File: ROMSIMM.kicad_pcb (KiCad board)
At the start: 4 copper layers, 88.9 x 19 mm, 8 parts, among them J1 Conn_01x30, U1 511400, U2 511400

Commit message: asdsda
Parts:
- removed the C3 at (118.6, 92.7)
- removed the C3 at (140.2, 92.7)
- added C3: 10u, stdpads:C_0805, F.Cu at (161.8, 105.9)
- added C5: 2u2, stdpads:C_0603, F.Cu at (120.7, 123.4)
- added C6: 2u2, stdpads:C_0603, F.Cu at (120.7, 104.6)
- added H1: MountingHole, Conn:MH_125, F.Cu at (75.1, 117.5)
- added H2: MountingHole, Conn:MH_125, F.Cu at (166.2, 117.5)
- added U3: D15-8, stdpads:PLCC-32_SMDSocket, F.Cu at (130.8, 113.0)
- added U4: D7-0, stdpads:PLCC-32_SMDSocket, F.Cu at (151.1, 113.0)
- C1, C2, C4: value 100n -> 10u; footprint stdpads:C_1206 -> stdpads:C_0805
- J1: value Conn_01x30 -> ROM; footprint stdpads:SIMM-30_Edge -> stdpads:MacIIROMSIMM_Edge
- U1: value 511400 -> D31-24; footprint stdpads:SOJ-24-26-300mil -> stdpads:PLCC-32_SMDSocket
- U2: value 511400 -> D23-16; footprint stdpads:SOJ-24-26-300mil -> stdpads:PLCC-32_SMDSocket
- moved U1 45.8 mm to (90.2, 113.0), turned to 0 degrees
- moved C2 39.5 mm to (79.5, 121.9)
- moved C4 29.2 mm to (161.8, 121.5)
- moved U2 27.9 mm to (110.5, 113.0), turned to 0 degrees
- moved J1 27.8 mm to (120.7, 127.6)
- moved C1 14.2 mm to (79.5, 105.9), turned to 270 degrees
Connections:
- J1 pad 10: /D2 -> GND
- J1 pad 11: /1A6 -> /~CS~
- J1 pad 12: /1A1 -> /~OE~
- J1 pad 13: /D3 -> /~WE~
- J1 pad 14: /1A7 -> /D0
- J1 pad 15: /1A0 -> /D1
- J1 pad 16: /D4 -> /D2
- J1 pad 17: /1A8 -> /D3
- J1 pad 18: /1A10 -> /D4
- J1 pad 19: /1A9 -> /D5
- J1 pad 2: /~CAS~ -> /A0
- J1 pad 20: /D5 -> /D6
- J1 pad 21: /~WE~ -> /D7
- J1 pad 22: GND -> /D8
- J1 pad 23: /D6 -> /D9
- J1 pad 24: /A11 -> /D10
- J1 pad 25: /D7 -> /D11
- J1 pad 26: /QP -> /D12
- J1 pad 27: /~RAS~ -> /D13
- J1 pad 28: /~CASP~ -> /D14
- J1 pad 29: /DP -> /D15
- J1 pad 3: /D0 -> /A1
- J1 pad 30: +5V -> GND
- J1 pad 4: /1A4 -> /A2
- J1 pad 5: /1A3 -> /A3
- J1 pad 6: /D1 -> /A4
- J1 pad 7: /1A5 -> /A5
- J1 pad 8: /1A2 -> /A6
- J1 pad 9: GND -> /A7
- U1 pad 1: +5V -> /A20
- U1 pad 10: /1A1 -> /A4
- U1 pad 11: /1A2 -> /A3
- U1 pad 12: /1A3 -> /A2
- U1 pad 13: +5V -> /D0
- U1 pad 14: GND -> /D1
- U1 pad 15: /1A4 -> /D2
- U1 pad 16: /1A5 -> GND
- U1 pad 17: /1A6 -> /D3
- U1 pad 18: /1A7 -> /D4
- U1 pad 19: /1A8 -> /D5
- U1 pad 2: /D5 -> /A18
- U1 pad 21: /1A9 -> /D7
- U1 pad 22: GND -> /~CS~
- U1 pad 23: /~CAS~ -> /A12
- U1 pad 24: /D6 -> /~OE~
- U1 pad 25: /D4 -> /A13
- U1 pad 26: GND -> /A11
- U1 pad 3: /D7 -> /A17
- U1 pad 4: /~WE~ -> /A14
- U1 pad 5: /~RAS~ -> /A9
- U1 pad 6: Net-(U1-Pad6) -> /A8
- U1 pad 8: /1A10 -> /A6
- U1 pad 9: /1A0 -> /A5
- U2 pad 1: +5V -> /A20
- U2 pad 10: /1A1 -> /A4
- U2 pad 11: /1A0 -> /A3
- U2 pad 12: /1A10 -> /A2
- U2 pad 13: +5V -> /D8
- U2 pad 14: GND -> /D9
- U2 pad 15: /1A9 -> /D10
- U2 pad 16: /1A8 -> GND
- U2 pad 17: /1A7 -> /D11
- U2 pad 18: /1A6 -> /D12
- U2 pad 19: /1A5 -> /D13
- U2 pad 2: /D1 -> /A18
- U2 pad 21: /1A4 -> /D15
- U2 pad 22: GND -> /~CS~
- U2 pad 23: /~CAS~ -> /A12
- U2 pad 24: /D2 -> /~OE~
- U2 pad 25: /D0 -> /A13
- U2 pad 26: GND -> /A11
- U2 pad 3: /D3 -> /A17
- U2 pad 4: /~WE~ -> /A14
- U2 pad 5: /~RAS~ -> /A9
- U2 pad 6: Net-(U2-Pad6) -> /A8
- U2 pad 8: /1A3 -> /A6
- U2 pad 9: /1A2 -> /A5
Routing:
- net +5V: track 29.6 -> 234.6 mm, vias 14 -> 28
- net /A20: track 0.00 -> 106.3 mm, vias 0 -> 4
- net /A14: track 0.00 -> 101.8 mm, vias 0 -> 5
- net /A19: track 0.00 -> 100.8 mm, vias 0 -> 4
- net /A17: track 0.00 -> 94.9 mm, vias 0 -> 6
- net /A18: track 0.00 -> 94.4 mm, vias 0 -> 6
- net /A16: track 0.00 -> 85.2 mm, vias 0 -> 1
- net /A15: track 0.00 -> 82.7 mm, vias 0 -> 1
- net /A7: track 0.00 -> 80.3 mm, vias 0 -> 1
- net /A9: track 0.00 -> 80.3 mm, vias 0 -> 1
- net /A10: track 0.00 -> 79.9 mm, vias 0 -> 1
- net /A11: track 0.00 -> 78.9 mm, vias 0 -> 1
- net /A13: track 0.00 -> 78.8 mm, vias 0 -> 1
- net /A8: track 0.00 -> 78.7 mm, vias 0 -> 1
- net /A6: track 0.00 -> 78.5 mm, vias 0 -> 1
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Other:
- board size 88.9 x 19 mm -> 97.8 x 26 mm
- board text added: "4401A"
- board text added: "GW"
- board text added: "Garrett’s Workshop"
- board text added: "ROM SIMM"
- board text added: "for Mac II and SE/30"

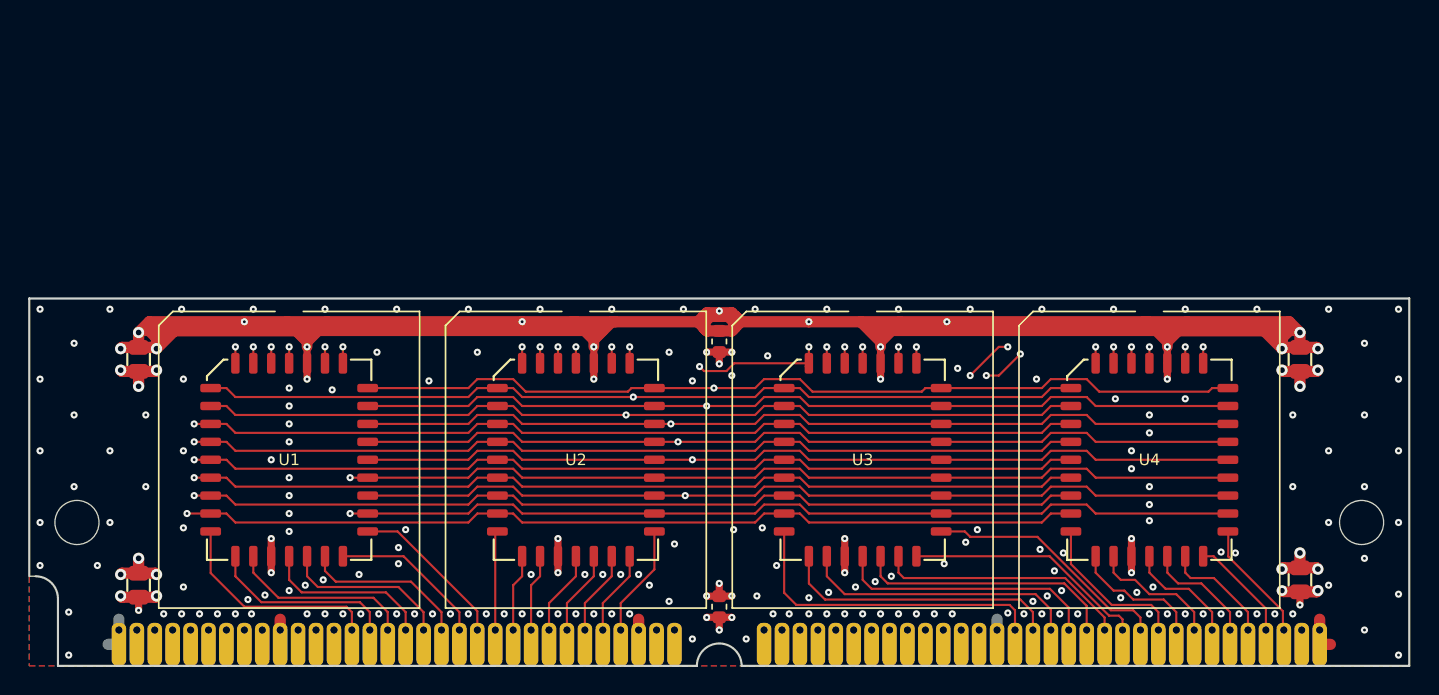
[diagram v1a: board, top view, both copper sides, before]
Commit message: Better stitching, with refdes on back
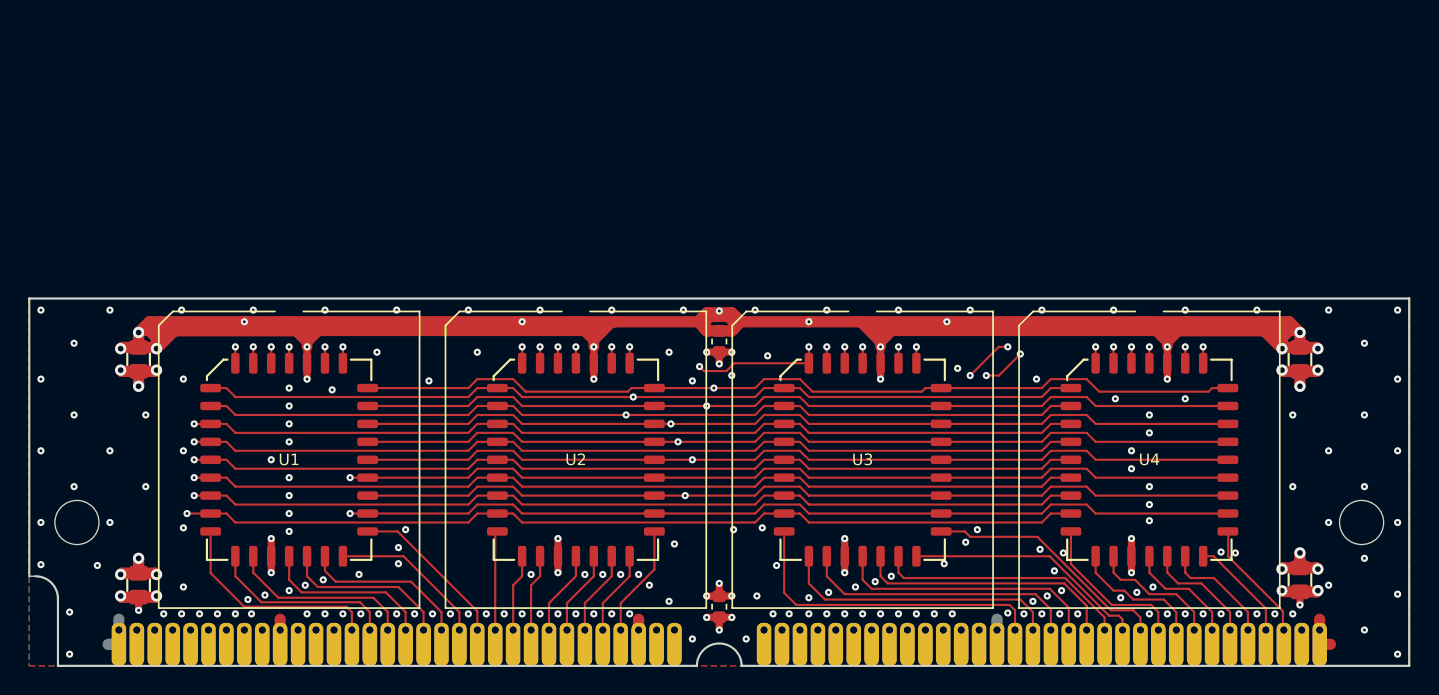
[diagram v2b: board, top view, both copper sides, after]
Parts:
- added ?: , , F.Cu at (90.2, 113.0)
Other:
- board text added: "U1"
- board text added: "U2"
- board text added: "U3"
- board text added: "U4"
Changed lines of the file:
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@@
   (general
     (thickness 1.6)
-    (drawings 16)
+    (drawings 20)
     (tracks 1087)
     (zones 0)
-    (modules 13)
+    (modules 14)
     (nets 62)
   )
@@
     (add_net GND)
     (add_net "Net-(J1-Pad63)")
+  )
+  (module "" (layer F.Cu)
+    (at 90.17 113.03)
+    (fp_text reference "" (at 120.65 127.635) (layer F.SilkS)
+      (effects (font (size 1.27 1.27) (thickness 0.15)))
+    )
+    (fp_text value "" (at 120.65 127.635) (layer F.SilkS)
+      (effects (font (size 1.27 1.27) (thickness 0.15)))
+    )
+    (fp_text user %R (at 120.65 127.635) (layer F.SilkS)
+      (effects (font (size 0.8128 0.8128) (thickness 0.2032)))
+    )
   )
   (module stdpads:MacIIROMSIMM_Edge (layer F.Cu)
@@
       (rotate (xyz 0 0 0))
     )
+  )
+  (gr_text U4 (at 151.13 120.015) (layer B.SilkS)
+    (effects (font (size 0.8128 0.8128) (thickness 0.2032)) (justify mirror))
+  )
+  (gr_text U3 (at 130.81 120.015) (layer B.SilkS)
+    (effects (font (size 0.8128 0.8128) (thickness 0.2032)) (justify mirror))
+  )
+  (gr_text U2 (at 110.49 120.015) (layer B.SilkS)
+    (effects (font (size 0.8128 0.8128) (thickness 0.2032)) (justify mirror))
+  )
+  (gr_text U1 (at 90.17 120.015) (layer B.SilkS)
+    (effects (font (size 0.8128 0.8128) (thickness 0.2032)) (justify mirror))
   )
   (gr_poly (pts (xy 163.195 127.635) (xy 123.825 127.635) (xy 123.317 125.0315) (xy 163.703 125.0315)) (layer F.Mask) (width 0.175))
@@
   (via (at 121.539 107.061) (size 0.508) (drill 0.2) (layers F.Cu B.Cu) (net 7))
   (via (at 143.129 107.315) (size 0.508) (drill 0.2) (layers F.Cu B.Cu) (net 7))
-  (via (at 72.517 102.362) (size 0.508) (drill 0.2) (layers F.Cu B.Cu) (net 7))
-  (via (at 77.47 102.362) (size 0.508) (drill 0.2) (layers F.Cu B.Cu) (net 7))
-  (via (at 82.55 102.362) (size 0.508) (drill 0.2) (layers F.Cu B.Cu) (net 7))
-  (via (at 87.63 102.362) (size 0.508) (drill 0.2) (layers F.Cu B.Cu) (net 7))
-  (via (at 92.71 102.362) (size 0.508) (drill 0.2) (layers F.Cu B.Cu) (net 7))
-  (via (at 97.79 102.362) (size 0.508) (drill 0.2) (layers F.Cu B.Cu) (net 7))
-  (via (at 148.59 102.362) (size 0.508) (drill 0.2) (layers F.Cu B.Cu) (net 7))
-  (via (at 158.75 102.362) (size 0.508) (drill 0.2) (layers F.Cu B.Cu) (net 7))
-  (via (at 143.51 102.362) (size 0.508) (drill 0.2) (layers F.Cu B.Cu) (net 7))
-  (via (at 168.783 102.362) (size 0.508) (drill 0.2) (layers F.Cu B.Cu) (net 7))
-  (via (at 163.83 102.362) (size 0.508) (drill 0.2) (layers F.Cu B.Cu) (net 7))
-  (via (at 153.67 102.362) (size 0.508) (drill 0.2) (layers F.Cu B.Cu) (net 7))
-  (via (at 102.87 102.362) (size 0.508) (drill 0.2) (layers F.Cu B.Cu) (net 7))
-  (via (at 107.95 102.362) (size 0.508) (drill 0.2) (layers F.Cu B.Cu) (net 7))
-  (via (at 138.43 102.362) (size 0.508) (drill 0.2) (layers F.Cu B.Cu) (net 7))
-  (via (at 133.35 102.362) (size 0.508) (drill 0.2) (layers F.Cu B.Cu) (net 7))
-  (via (at 128.27 102.362) (size 0.508) (drill 0.2) (layers F.Cu B.Cu) (net 7))
-  (via (at 113.03 102.362) (size 0.508) (drill 0.2) (layers F.Cu B.Cu) (net 7))
-  (via (at 118.11 102.362) (size 0.508) (drill 0.2) (layers F.Cu B.Cu) (net 7))
-  (via (at 123.19 102.362) (size 0.508) (drill 0.2) (layers F.Cu B.Cu) (net 7))
-  (via (at 72.517 107.315) (size 0.508) (drill 0.2) (layers F.Cu B.Cu) (net 7))
-  (via (at 72.517 112.395) (size 0.508) (drill 0.2) (layers F.Cu B.Cu) (net 7))
-  (via (at 72.517 117.475) (size 0.508) (drill 0.2) (layers F.Cu B.Cu) (net 7))
-  (via (at 72.517 120.523) (size 0.508) (drill 0.2) (layers F.Cu B.Cu) (net 7))
-  (via (at 74.549 126.873) (size 0.508) (drill 0.2) (layers F.Cu B.Cu) (net 7))
-  (via (at 168.783 126.873) (size 0.508) (drill 0.2) (layers F.Cu B.Cu) (net 7))
-  (via (at 168.783 107.315) (size 0.508) (drill 0.2) (layers F.Cu B.Cu) (net 7))
-  (via (at 168.783 112.395) (size 0.508) (drill 0.2) (layers F.Cu B.Cu) (net 7))
-  (via (at 168.783 117.475) (size 0.508) (drill 0.2) (layers F.Cu B.Cu) (net 7))
-  (via (at 168.783 122.555) (size 0.508) (drill 0.2) (layers F.Cu B.Cu) (net 7))
-  (via (at 74.549 123.825) (size 0.508) (drill 0.2) (layers F.Cu B.Cu) (net 7))
+  (via (at 72.5805 102.4255) (size 0.508) (drill 0.2) (layers F.Cu B.Cu) (net 7))
+  (via (at 77.47 102.4255) (size 0.508) (drill 0.2) (layers F.Cu B.Cu) (net 7))
+  (via (at 82.55 102.4255) (size 0.508) (drill 0.2) (layers F.Cu B.Cu) (net 7))
+  (via (at 87.63 102.4255) (size 0.508) (drill 0.2) (layers F.Cu B.Cu) (net 7))
+  (via (at 92.71 102.4255) (size 0.508) (drill 0.2) (layers F.Cu B.Cu) (net 7))
+  (via (at 97.79 102.4255) (size 0.508) (drill 0.2) (layers F.Cu B.Cu) (net 7))
+  (via (at 148.59 102.4255) (size 0.508) (drill 0.2) (layers F.Cu B.Cu) (net 7))
+  (via (at 158.75 102.4255) (size 0.508) (drill 0.2) (layers F.Cu B.Cu) (net 7))
+  (via (at 143.51 102.4255) (size 0.508) (drill 0.2) (layers F.Cu B.Cu) (net 7))
+  (via (at 168.7195 102.4255) (size 0.508) (drill 0.2) (layers F.Cu B.Cu) (net 7))
+  (via (at 163.83 102.4255) (size 0.508) (drill 0.2) (layers F.Cu B.Cu) (net 7))
+  (via (at 153.67 102.4255) (size 0.508) (drill 0.2) (layers F.Cu B.Cu) (net 7))
+  (via (at 102.87 102.4255) (size 0.508) (drill 0.2) (layers F.Cu B.Cu) (net 7))
+  (via (at 107.95 102.4255) (size 0.508) (drill 0.2) (layers F.Cu B.Cu) (net 7))
+  (via (at 138.43 102.4255) (size 0.508) (drill 0.2) (layers F.Cu B.Cu) (net 7))
+  (via (at 133.35 102.4255) (size 0.508) (drill 0.2) (layers F.Cu B.Cu) (net 7))
+  (via (at 128.27 102.4255) (size 0.508) (drill 0.2) (layers F.Cu B.Cu) (net 7))
+  (via (at 113.03 102.4255) (size 0.508) (drill 0.2) (layers F.Cu B.Cu) (net 7))
+  (via (at 118.11 102.4255) (size 0.508) (drill 0.2) (layers F.Cu B.Cu) (net 7))
+  (via (at 123.19 102.4255) (size 0.508) (drill 0.2) (layers F.Cu B.Cu) (net 7))
+  (via (at 72.5805 107.315) (size 0.508) (drill 0.2) (layers F.Cu B.Cu) (net 7))
+  (via (at 72.5805 112.395) (size 0.508) (drill 0.2) (layers F.Cu B.Cu) (net 7))
+  (via (at 72.5805 117.475) (size 0.508) (drill 0.2) (layers F.Cu B.Cu) (net 7))
+  (via (at 72.5805 120.4595) (size 0.508) (drill 0.2) (layers F.Cu B.Cu) (net 7))
+  (via (at 74.6125 126.8095) (size 0.508) (drill 0.2) (layers F.Cu B.Cu) (net 7))
+  (via (at 168.7195 126.8095) (size 0.508) (drill 0.2) (layers F.Cu B.Cu) (net 7))
+  (via (at 168.7195 107.315) (size 0.508) (drill 0.2) (layers F.Cu B.Cu) (net 7))
+  (via (at 168.7195 112.395) (size 0.508) (drill 0.2) (layers F.Cu B.Cu) (net 7))
+  (via (at 168.7195 117.475) (size 0.508) (drill 0.2) (layers F.Cu B.Cu) (net 7))
+  (via (at 168.7195 122.555) (size 0.508) (drill 0.2) (layers F.Cu B.Cu) (net 7))
+  (via (at 74.6125 123.825) (size 0.508) (drill 0.2) (layers F.Cu B.Cu) (net 7))
   (via (at 120.65 125.095) (size 0.508) (drill 0.2) (layers F.Cu B.Cu) (net 7))
   (via (at 118.745 125.73) (size 0.508) (drill 0.2) (layers F.Cu B.Cu) (net 7))

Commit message: Rounded corners
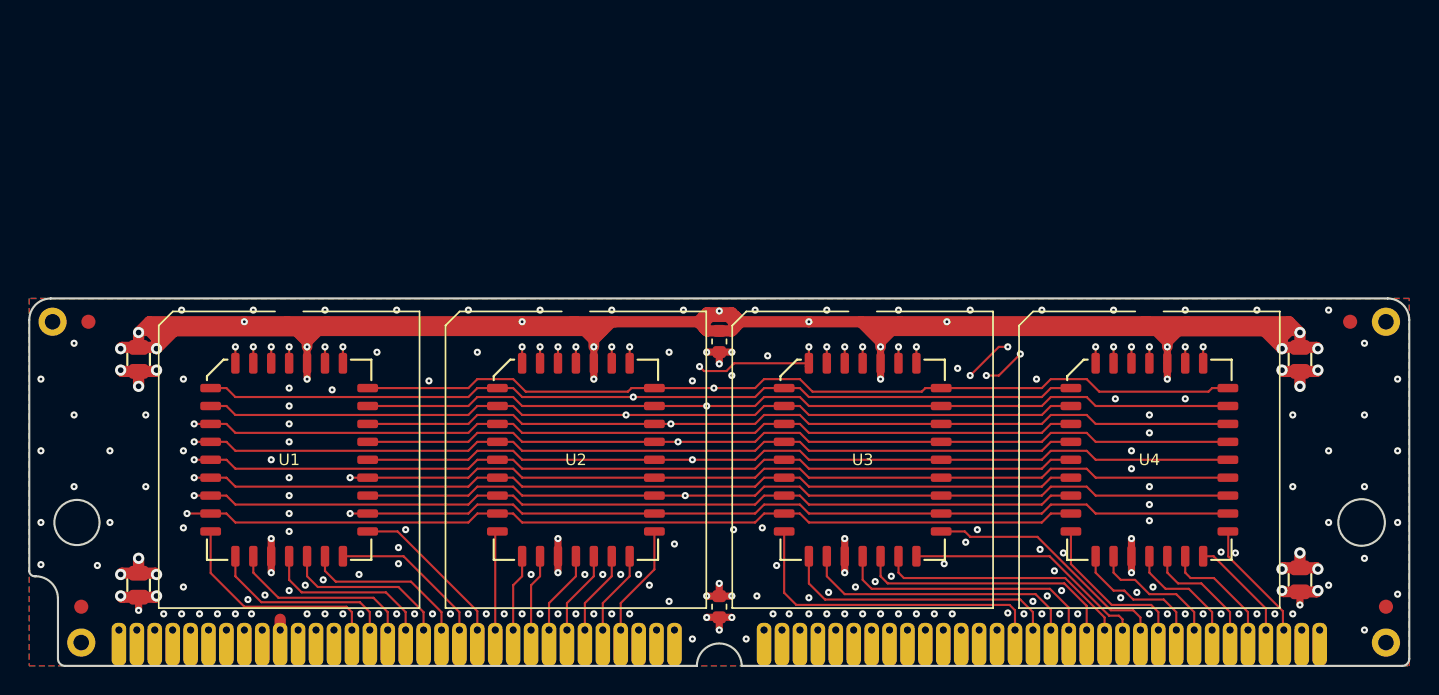
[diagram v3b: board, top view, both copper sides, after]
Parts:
- added FID1: Fiducial, stdpads:Fiducial, F.Cu at (75.9, 103.3)
- added FID2: Fiducial, stdpads:Fiducial, F.Cu at (75.4, 123.4)
- added FID3: Fiducial, stdpads:Fiducial, F.Cu at (167.9, 123.4)
- added FID4: Fiducial, stdpads:Fiducial, F.Cu at (165.4, 103.3)
- added H3: , stdpads:PasteHole_1.1mm_PTH, F.Cu at (167.9, 126.0)
- added H4: , stdpads:PasteHole_1.1mm_PTH, F.Cu at (167.9, 103.3)
- H1, H2: value MountingHole -> (none); footprint Conn:MH_125 -> stdpads:PasteHole_1.1mm_PTH
- moved H2 91.1 mm to (75.4, 126.0)
- moved H1 14.3 mm to (73.4, 103.3)
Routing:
- net GND: track 41.8 -> 31.9 mm, vias 199 -> 193
- net +5V: track 234.6 -> 231.3 mm
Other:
- outline, holes or cut-outs redrawn
